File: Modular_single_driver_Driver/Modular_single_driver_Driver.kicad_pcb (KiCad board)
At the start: 2 copper layers, 64.4 x 30.6 mm, 31 parts, among them J1 Conn_02x02_Counter_Clockwise, J2 Screw_Terminal_01x02, J3 Conn_01x08_Male, J4 Conn_01x03_Male, SW1 SW_DIP_x06, U2 LM7805_TO220, U3 DRV10970

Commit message: More
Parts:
- removed C1, C2, C4: 0.1u, Capacitor_SMD:C_0603_1608Metric
- removed C3: 0.33u, Capacitor_SMD:C_0603_1608Metric
- removed D2: LED, LED_SMD:LED_1206_3216Metric
- removed J2: Screw_Terminal_01x02, TerminalBlock_Phoenix:TerminalBlock_Phoenix_PT-1,5-2-3.5-H_1x02_P3.50mm_Horizontal
- removed R4: 510, Resistor_SMD:R_0603_1608Metric
- removed U2: LM7805_TO220, Package_TO_SOT_THT:TO-220-3_Vertical
- moved C5 19.2 mm to (178.5, 125.0)
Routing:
- net +12V: track 59.0 -> 0.00 mm
- net GND: track 95.5 -> 60.2 mm
- net +5V: track 57.6 -> 50.7 mm, vias 7 -> 6
- net Net-(D2-Pad1): track 2.16 -> 0.00 mm
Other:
- outline, holes or cut-outs redrawn
- board text added: "+"
- board text added: "-"
- board text added: "BRK"
- board text added: "CMT"
- board text added: "DAA"
- board text added: "FG"
- board text added: "FR"
- board text added: "GND"
- board text added: "RD"

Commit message: Yes they are
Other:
- board text added: "+5V"
- board text added: "ADC"
- board text added: "PWM"

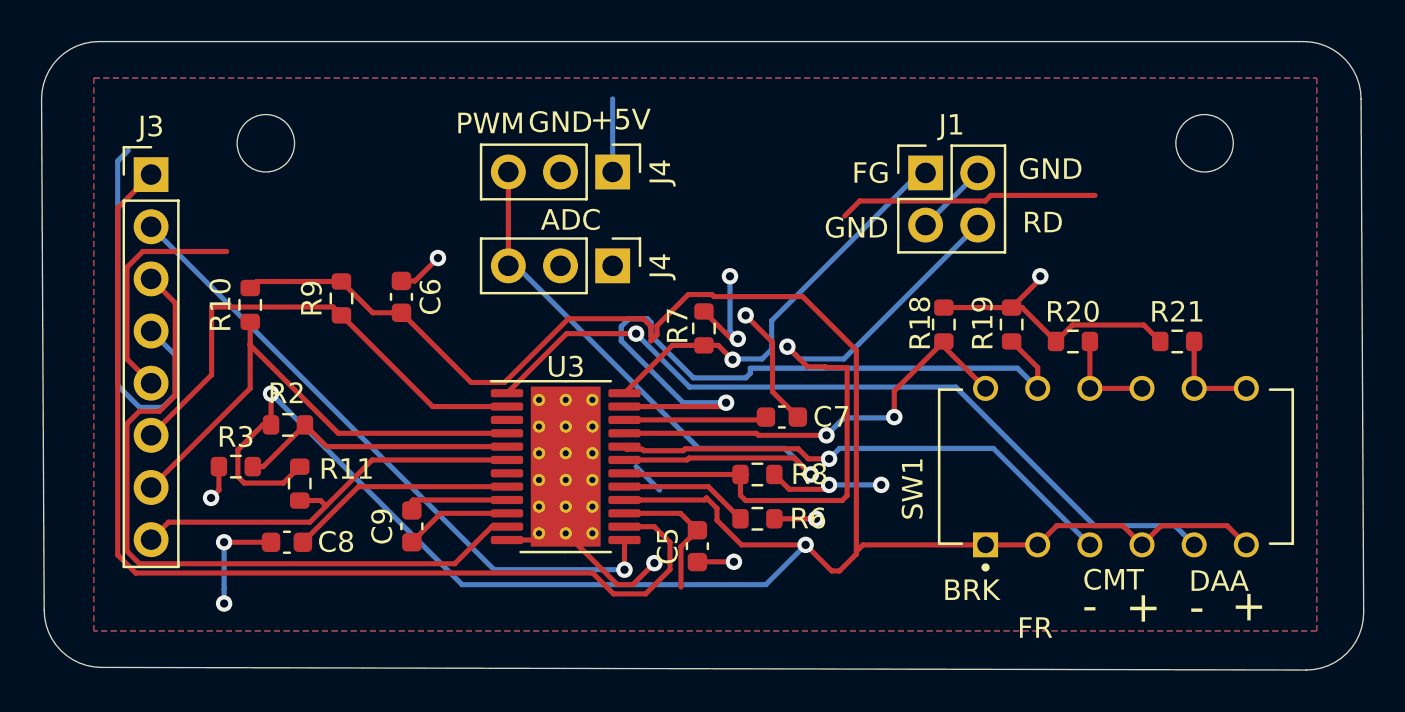
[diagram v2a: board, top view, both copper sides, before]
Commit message: Updated connections and component values
- Updated component values to reflect those shown in the datasheet
- Connected HBIAS pins to each other
- Connected PowerPAD to ground plane
- Cleaned up traces
- Added some silkscreen labels to facilitate testing
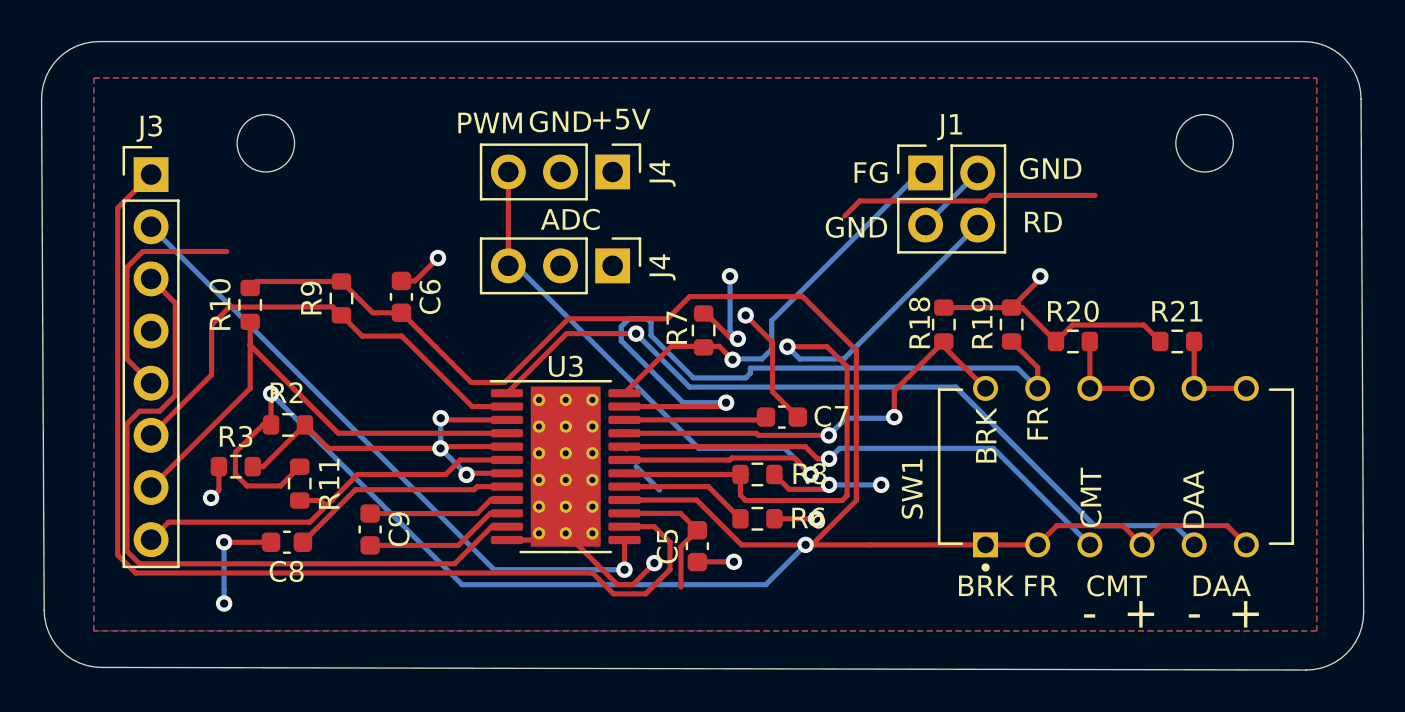
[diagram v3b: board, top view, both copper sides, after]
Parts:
- C5: value 1u -> 10uF
- C6: value 2.2u -> 2.2uF
- C7, C8: value 1u -> 1uF
- C9: value 0.1u -> 0.1uF
- R6: value 200k -> 24k
- R7, R8: value 10k -> 3.3k
- moved C9 2.04 mm to (162.6, 124.2)
- moved R7 0.10 mm to (178.8, 114.5)
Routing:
- net GND: track 60.2 -> 41.5 mm
- net /HBIAS: track 13.7 -> 22.5 mm, vias 0 -> 3
- net +5V: track 50.7 -> 47.2 mm
- net Net-(C9-Pad1): track 5.21 -> 7.31 mm
- net /VINT: track 120.1 -> 118.1 mm
- net Net-(C9-Pad2): track 5.10 -> 6.94 mm
- net /HU: track 23.9 -> 23.3 mm
